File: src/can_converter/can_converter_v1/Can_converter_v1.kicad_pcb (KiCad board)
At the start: 2 copper layers, 37.7 x 20 mm, 44 parts, among them P1 CONN_01X02, P2 CONN_01X02, T101 Tab, T102 Tab, T103 Tab, T104 Tab, U1 STM32G0B1CBT, U2 MCP1754ST-3302E/MB, U3 TJA1051T3, U4 TJA1051T3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

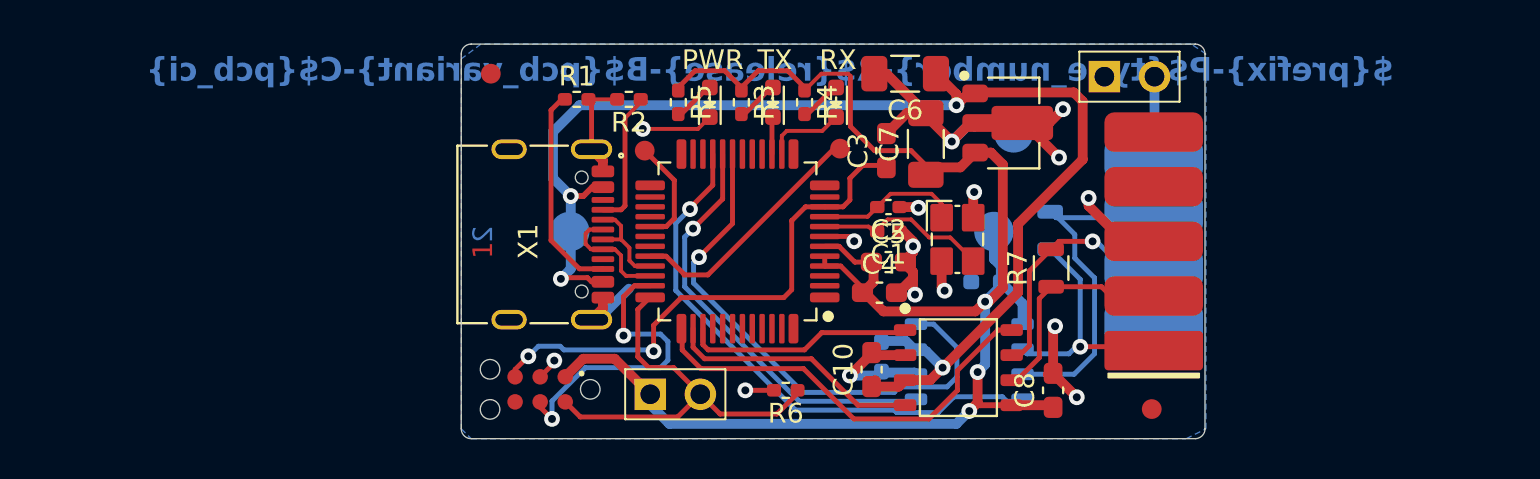
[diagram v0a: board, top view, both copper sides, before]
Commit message: Replace regulator and tranceiver
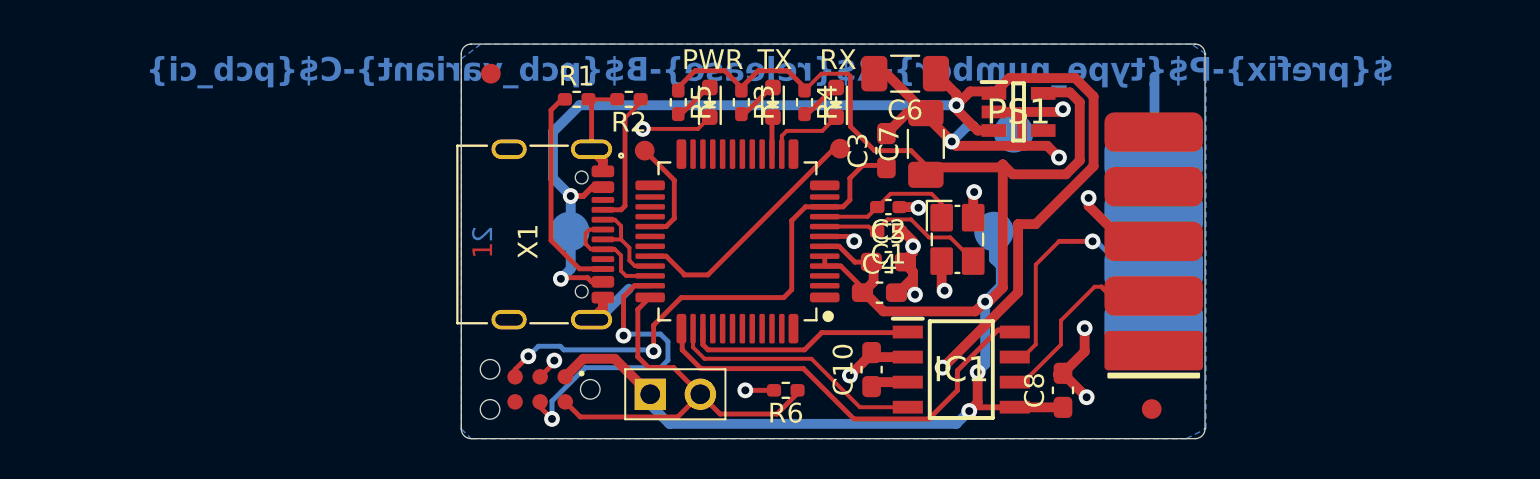
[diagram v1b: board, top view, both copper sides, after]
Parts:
- removed C11, C9: 100n_0603_X7R_10%_50V_-40C..125C_Chip-Capacitor, Capacitors_SMD:C_0603
- removed P1: CONN_01X02, Connector_generic:Header_1x2_Pitch2.54mm
- removed R7, R8: 120R_0805_125mW_1%_E24_Chip-Resistor, Resistors_SMD:R_0805
- removed U2: MCP1754ST-3302E/MB, TO_SMD:SOT-89
- removed U3, U4: TJA1051T3, tssop:SOIC-8_3.90mmx4.90mm_Pitch1.27mm
- added IC1: TCAN1462VDRQ1, footprints:SOIC127P600X175-8N, F.Cu at (126.3, 136.5)
- added PS1: RT9013-33GB, footprints:SOT94P279X130-5N, F.Cu at (129.2, 123.4)
- moved C8 0.50 mm to (131.5, 137.6)
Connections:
- U1 pad 19: /CAN Transceiver/CAN2_RX -> /MCU/CAN2_RX
- U1 pad 20: /CAN Transceiver/CAN2_TX -> /MCU/CAN2_TX
- U1 pad 21: /CAN Transceiver/CAN2_S -> /MCU/CAN2_S
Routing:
- net /CAN Transceiver/CAN2_S: track 28.3 -> 0.00 mm, vias 1 -> 0
- net /CAN Transceiver/CAN2_RX: track 27.4 -> 0.00 mm, vias 1 -> 0
- net /CAN Transceiver/CAN2_TX: track 21.7 -> 0.00 mm, vias 1 -> 0
- net /CAN2_H: track 17.7 -> 0.26 mm
- net /CAN2_L: track 12.6 -> 1.50 mm, vias 1 -> 0
- net +3V3: track 83.5 -> 90.8 mm
- net GND: track 58.2 -> 61.1 mm
- net +5V: track 66.4 -> 65.0 mm
- net /CAN1_L: track 11.3 -> 10.4 mm
